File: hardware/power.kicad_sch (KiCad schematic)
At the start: 61 parts, among them IC1 LMR38020FDDAR, Q1 LMR51635XDDCR, Q2 LMR51635XDDCR, U3 LM1117-3.3

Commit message: Table updated- fuses and conns still not added
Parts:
- C10, C11, C13, C14, C15, C26, C30, C31: Mouser Price/Stock (none) -> https://www.mouser.pl/ProductDetail/KEMET/C0603C104J5RACTM?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
- C12, C19, C24, C25, C32, C33: Mouser Price/Stock (none) -> https://www.mouser.pl/ProductDetail/Murata-Electronics/GRM3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
- C16, C17, C27, C28, C29, C5: Mouser Price/Stock (none) -> https://www.mouser.pl/ProductDetail/TAIYO-YUDEN/MMJCG168CB7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
- C20, C22: footprint Capacitor_SMD:CP_Elec_4x5.8 -> SamacSys_Parts:CAPPM7343X310N; Mouser Price/Stock https://www.mouser.pl/ProductDetail/Samsung-Electro-Mechani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 -> https://www.mouser.pl/ProductDetail/TDK/C2012X5R1V226M125AC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
- C21, C23, C9: Mouser Price/Stock (none) -> https://www.mouser.pl/ProductDetail/Murata-Electronics/GRM1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
- D2: Mouser Price/Stock (none) -> https://www.mouser.pl/ProductDetail/Diotec-Semiconductor/SK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
- D3, D4: Mouser Price/Stock (none) -> https://www.we-online.com/components/products/datasheet/150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
- L1: Mouser Price/Stock (none) -> https://www.mouser.pl/ProductDetail/Bourns/SRU1028A-150Y?qs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
- L2, L3: Mouser Price/Stock (none) -> https://www.mouser.pl/ProductDetail/Bourns/SRR1206-120ML?qs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
- Q1, Q2: Mouser Price/Stock (none) -> https://www.mouser.pl/ProductDetail/Texas-Instruments/LMR51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
- R10: Mouser Price/Stock (none) -> https://www.mouser.pl/ProductDetail/Vishay-Dale/CRCW060310K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
- R11, R13: Mouser Price/Stock (none) -> https://www.mouser.pl/ProductDetail/YAGEO/AC0603DRE0713K7L?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
- R12, R5: Mouser Price/Stock (none) -> https://www.mouser.pl/ProductDetail/KOA-Speer/RK73B1JTTD104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
- R14, R8: Mouser Price/Stock (none) -> https://www.mouser.pl/ProductDetail/Vishay-Dale/CRCW06031K0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
- R7: Mouser Price/Stock (none) -> https://www.mouser.pl/ProductDetail/Vishay-Beyschlag/MCT060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
- R9: Mouser Price/Stock (none) -> https://www.mouser.pl/ProductDetail/Panasonic/ERJ-S03F4022V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
- U3: Mouser Price/Stock (none) -> https://www.mouser.pl/ProductDetail/Texas-Instruments/LM111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

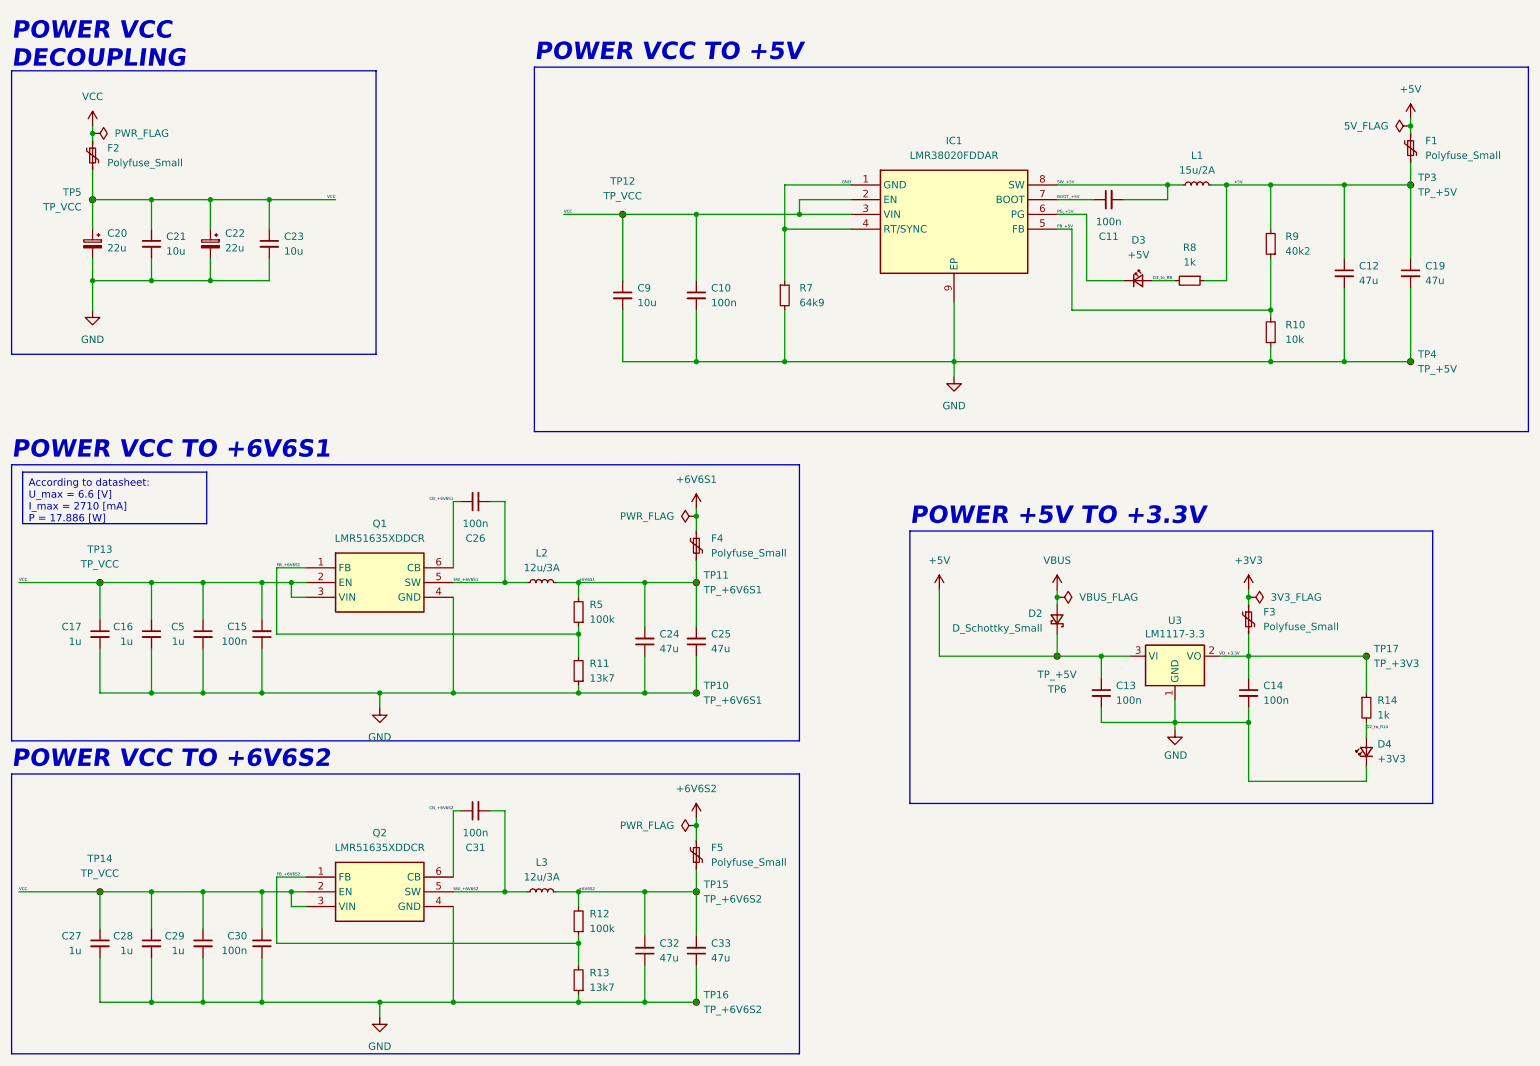
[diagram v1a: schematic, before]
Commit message: All footprints added
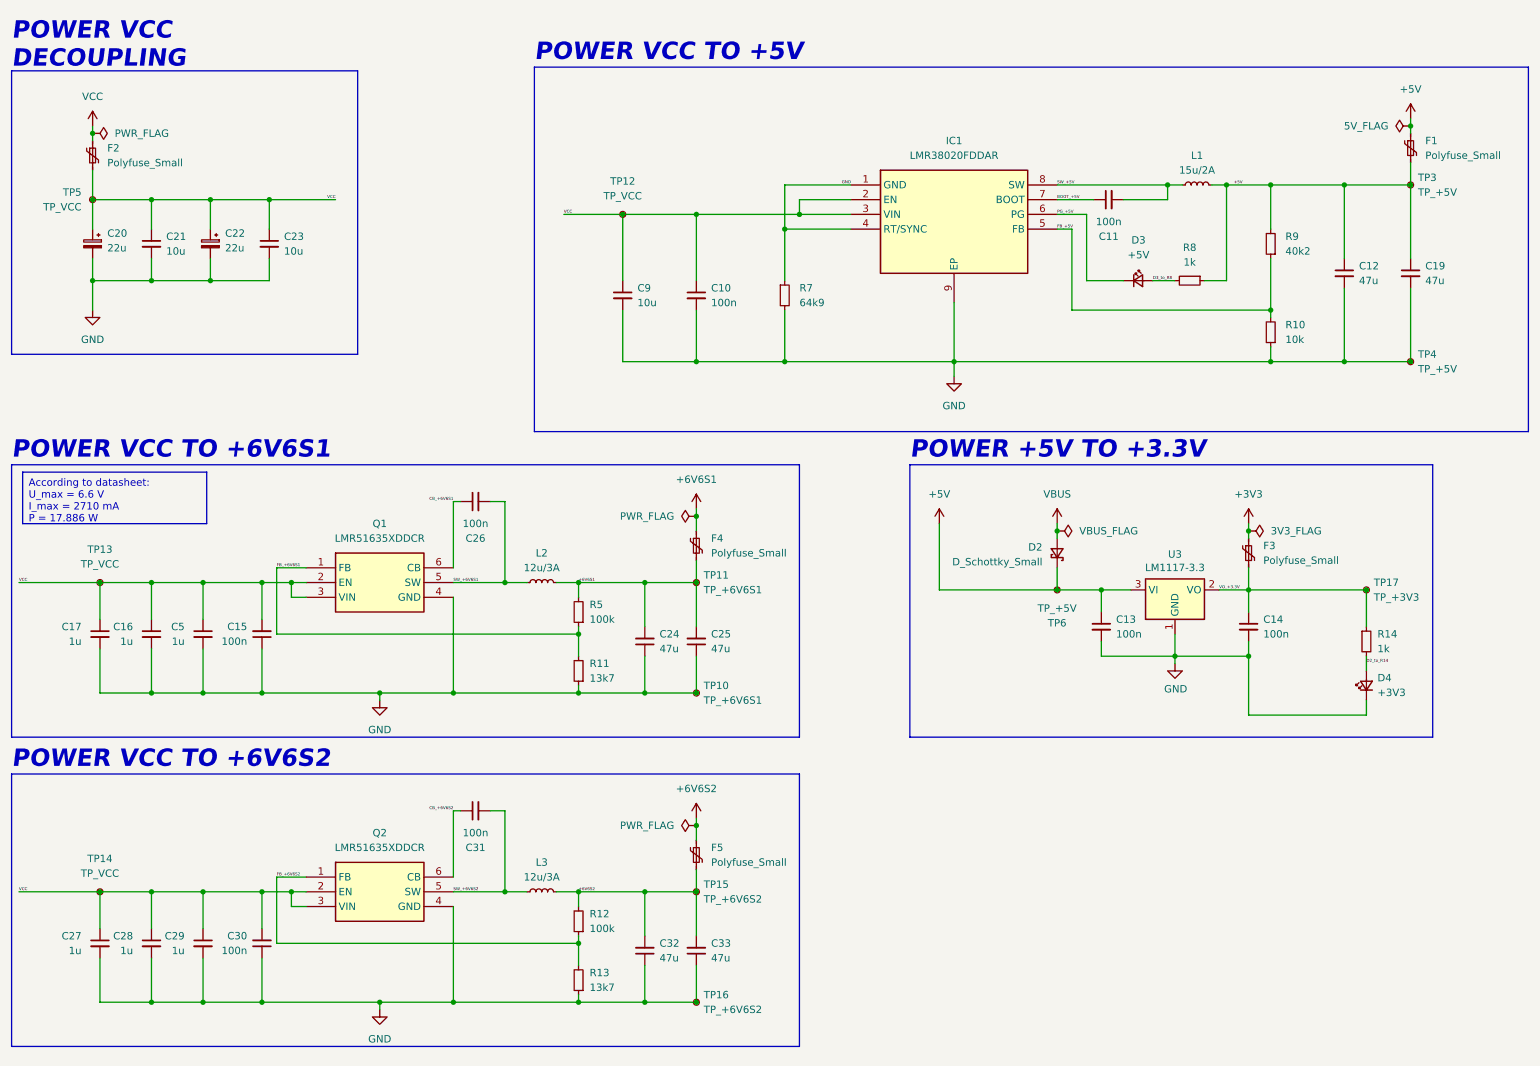
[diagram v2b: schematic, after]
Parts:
- F1, F3: footprint Fuse:Fuse_1206_3216Metric -> SamacSys_Parts:MINIASMDC260F162; Mouser Price/Stock (none) -> https://www.mouser.pl/ProductDetail/Littelfuse/MINIASMDC260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
- F2: footprint Fuse:Fuse_1206_3216Metric -> Fuse:Fuse_1206_3216Metric_Pad1.42x1.75mm_HandSolder; Mouser Price/Stock (none) -> https://www.mouser.pl/ProductDetail/Bourns/SF-1206HH800R-2?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
- F4, F5: footprint Fuse:Fuse_1206_3216Metric -> Fuse:Fuse_1206_3216Metric_Pad1.42x1.75mm_HandSolder; Mouser Price/Stock (none) -> https://www.mouser.pl/ProductDetail/Littelfuse/1206L150THWR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
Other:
- moved on the sheet: C13, C14, D2, D4, F3, R14, TP17, TP6, U3

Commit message: pcb scheme update - general/basic aligment
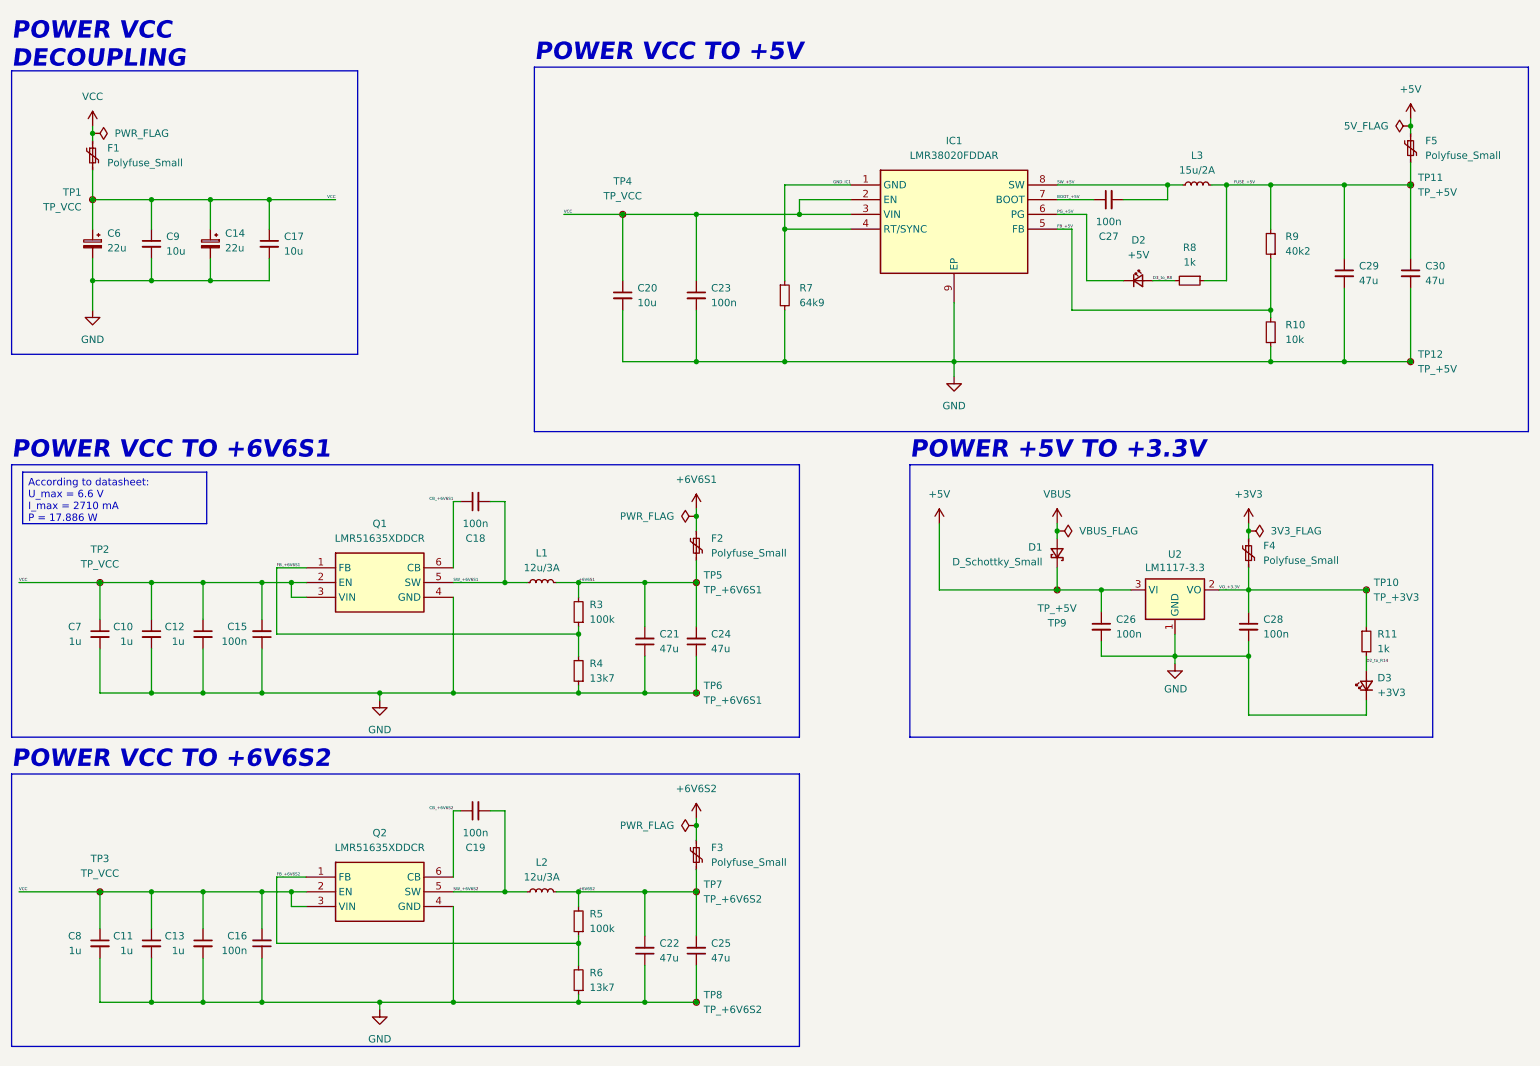
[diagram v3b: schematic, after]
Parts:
- F2: renamed from F4; footprint Fuse:Fuse_1206_3216Metric_Pad1.42x1.75mm_HandSolder -> Fuse:Fuse_0805_2012Metric_Pad1.15x1.40mm_HandSolder; Mouser Price/Stock https://www.mouser.pl/ProductDetail/Littelfuse/1206L150THWR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 -> https://www.mouser.pl/ProductDetail/Eaton-Electronics/PTSLR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
- F3: renamed from F5; footprint Fuse:Fuse_1206_3216Metric_Pad1.42x1.75mm_HandSolder -> Fuse:Fuse_0805_2012Metric_Pad1.15x1.40mm_HandSolder; Mouser Price/Stock https://www.mouser.pl/ProductDetail/Littelfuse/1206L150THWR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 -> https://www.mouser.pl/ProductDetail/Eaton-Electronics/PTSLR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
- L1: renamed from L2; footprint SamacSys_Parts:SRR1206120ML -> SamacSys_Parts:VLS6045; Mouser Price/Stock https://www.mouser.pl/ProductDetail/Bourns/SRR1206-120ML?qs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 -> https://www.mouser.pl/ProductDetail/TDK/VLS6045EX-150M?qs=o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
- L2: renamed from L3; footprint SamacSys_Parts:SRR1206120ML -> SamacSys_Parts:VLS6045; Mouser Price/Stock https://www.mouser.pl/ProductDetail/Bourns/SRR1206-120ML?qs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 -> https://www.mouser.pl/ProductDetail/TDK/VLS6045EX-150M?qs=o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
- L3: renamed from L1; footprint Inductor_SMD:L_Bourns-SRU1028_10.0x10.0mm -> SamacSys_Parts:VLS6045; Mouser Price/Stock https://www.mouser.pl/ProductDetail/Bourns/SRU1028A-150Y?qs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 -> https://www.mouser.pl/ProductDetail/TDK/VLS6045EX-150M?qs=o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
- renumbered C16 to C10, C28 to C11, C5 to C12, C29 to C13, C22 to C14, C30 to C16, C23 to C17, C26 to C18, C31 to C19, C9 to C20, C24 to C21, C32 to C22, C10 to C23, C25 to C24, C33 to C25, C13 to C26, C11 to C27, C14 to C28, C12 to C29, C19 to C30, C20 to C6, C17 to C7, C27 to C8, C21 to C9, D2 to D1, D3 to D2, D4 to D3, F2 to F1, F3 to F4, F1 to F5, R14 to R11, R5 to R3, R11 to R4, R12 to R5, R13 to R6, TP5 to TP1, TP17 to TP10, TP3 to TP11, TP4 to TP12, TP13 to TP2, TP14 to TP3, TP12 to TP4, TP11 to TP5, TP10 to TP6, TP15 to TP7, TP16 to TP8, TP6 to TP9, U3 to U2
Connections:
- net +5V: no longer C29.1, C30.1, F5.2, L3.2, R8.1, R9.2, TP11.1
- net GND: no longer IC1.1 (GND), IC1.4 (RT/SYNC), R7.1
- new net FUSE_+5V: C29.1, C30.1, F5.2, L3.2, R8.1, R9.2, TP11.1
- new net GND_IC1: IC1.1 (GND), IC1.4 (RT/SYNC), R7.1

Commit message: Items assebled
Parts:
- TP9: value TP_+5V -> T_+5V
- renumbered TP1 to T1, TP10 to T10, TP11 to T11, TP12 to T12, TP2 to T2, TP3 to T3, TP4 to T4, TP5 to T5, TP6 to T6, TP7 to T7, TP8 to T8
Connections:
- net +6V6S1: no longer C21.2, C24.2, F2.2, L1.2, R3.2, T5.1
- net +6V6S2: no longer C22.2, C25.2, F3.2, L2.2, R5.2, T7.1
- net VCC: no longer C14.1, C17.1, C6.1, C9.1, F1.2, T1.1
- new net +6V6S1_OUT: C21.2, C24.2, F2.2, L1.2, R3.2, T5.1
- new net +6V6S2_OUT: C22.2, C25.2, F3.2, L2.2, R5.2, T7.1
- new net VCC_IN: C14.1, C17.1, C6.1, C9.1, F1.2, T1.1
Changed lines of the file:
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@@
 		)
 	)
-	(label "VCC"
+	(label "VCC_IN"
 		(at 72.39 48.26 180)
 		(effects
@@
 		)
 	)
-	(label "+6V6S2"
+	(label "+6V6S2_OUT"
 		(at 114.3 167.64 0)
 		(effects
@@
 		)
 	)
-	(label "+6V6S1"
+	(label "+6V6S1_OUT"
 		(at 114.3 114.3 0)
 		(effects
@@
 			)
 		)
-		(property "Value" "TP_+5V"
+		(property "Value" "T_+5V"
 			(at 196.85 118.745 90)
 			(effects
@@
 		(dnp no)
 		(fields_autoplaced yes)
-		(property "Reference" "TP10"
+		(property "Reference" "T10"
 			(at 251.46 114.2999 0)
 			(effects
@@
 			(project "drs"
 				(path "/b652b05a-4e3d-4ad1-b032-18886abe7d45/29f85ecd-7b45-4817-8022-029f79a199a0"
-					(reference "TP10")
+					(reference "T10")
 					(unit 1)
 				)
@@
 		(on_board yes)
 		(dnp no)
-		(property "Reference" "TP1"
+		(property "Reference" "T1"
 			(at 28.575 46.9899 0)
 			(effects
@@
 			(project "drs"
 				(path "/b652b05a-4e3d-4ad1-b032-18886abe7d45/29f85ecd-7b45-4817-8022-029f79a199a0"
-					(reference "TP1")
+					(reference "T1")
 					(unit 1)
 				)
@@
 		(dnp no)
 		(fields_autoplaced yes)
-		(property "Reference" "TP8"
+		(property "Reference" "T8"
 			(at 135.89 185.4199 0)
 			(effects
@@
 			(project "drs"
 				(path "/b652b05a-4e3d-4ad1-b032-18886abe7d45/29f85ecd-7b45-4817-8022-029f79a199a0"
-					(reference "TP8")
+					(reference "T8")
 					(unit 1)
 				)
@@
 		(dnp no)
 		(fields_autoplaced yes)
-		(property "Reference" "TP12"
+		(property "Reference" "T12"
 			(at 259.08 74.9299 0)
 			(effects
@@
 			(project "drs"
 				(path "/b652b05a-4e3d-4ad1-b032-18886abe7d45/29f85ecd-7b45-4817-8022-029f79a199a0"
-					(reference "TP12")
+					(reference "T12")
 					(unit 1)
 				)
@@
 		(dnp no)
 		(fields_autoplaced yes)
-		(property "Reference" "TP3"
-			(at 31.75 161.925 90)
+		(property "Reference" "T3"
+			(at 31.75 162.56 90)
 			(effects
 				(font
@@
 		)
 		(property "Value" "TP_VCC"
-			(at 31.75 164.465 90)
+			(at 31.75 165.1 90)
 			(effects
 				(font
@@
 			(project "drs"
 				(path "/b652b05a-4e3d-4ad1-b032-18886abe7d45/29f85ecd-7b45-4817-8022-029f79a199a0"
-					(reference "TP3")
+					(reference "T3")
 					(unit 1)
 				)
@@
 		(dnp no)
 		(fields_autoplaced yes)
-		(property "Reference" "TP4"
-			(at 121.92 45.085 90)
+		(property "Reference" "T4"
+			(at 121.92 45.72 90)
 			(effects
 				(font
@@
 		)
 		(property "Value" "TP_VCC"
-			(at 121.92 47.625 90)
+			(at 121.92 48.26 90)
 			(effects
 				(font
@@
 			(project "drs"
 				(path "/b652b05a-4e3d-4ad1-b032-18886abe7d45/29f85ecd-7b45-4817-8022-029f79a199a0"
-					(reference "TP4")
+					(reference "T4")
 					(unit 1)
 				)
@@
 		(dnp no)
 		(fields_autoplaced yes)
-		(property "Reference" "TP7"
+		(property "Reference" "T7"
 			(at 135.89 166.3699 0)
 			(effects
@@
 			(project "drs"
 				(path "/b652b05a-4e3d-4ad1-b032-18886abe7d45/29f85ecd-7b45-4817-8022-029f79a199a0"
-					(reference "TP7")
+					(reference "T7")
 					(unit 1)
 				)
@@
 		(dnp no)
 		(fields_autoplaced yes)
-		(property "Reference" "TP6"
+		(property "Reference" "T6"
 			(at 135.89 132.0799 0)
 			(effects
@@
 			(project "drs"
 				(path "/b652b05a-4e3d-4ad1-b032-18886abe7d45/29f85ecd-7b45-4817-8022-029f79a199a0"
-					(reference "TP6")
+					(reference "T6")
 					(unit 1)
 				)
@@
 		(dnp no)
 		(fields_autoplaced yes)
-		(property "Reference" "TP2"
-			(at 31.75 108.585 90)
+		(property "Reference" "T2"
+			(at 31.75 109.22 90)
 			(effects
 				(font
@@
 		)
 		(property "Value" "TP_VCC"
-			(at 31.75 111.125 90)
+			(at 31.75 111.76 90)
 			(effects
 				(font
@@
 			(project "drs"
 				(path "/b652b05a-4e3d-4ad1-b032-18886abe7d45/29f85ecd-7b45-4817-8022-029f79a199a0"
-					(reference "TP2")
+					(reference "T2")
 					(unit 1)
 				)
@@
 		(dnp no)
 		(fields_autoplaced yes)
-		(property "Reference" "TP11"
+		(property "Reference" "T11"
 			(at 259.08 44.4499 0)
 			(effects
@@
 			(project "drs"
 				(path "/b652b05a-4e3d-4ad1-b032-18886abe7d45/29f85ecd-7b45-4817-8022-029f79a199a0"
-					(reference "TP11")
+					(reference "T11")
 					(unit 1)
 				)
@@
 		(dnp no)
 		(fields_autoplaced yes)
-		(property "Reference" "TP5"
+		(property "Reference" "T5"
 			(at 135.89 113.0299 0)
 			(effects
@@
 			(project "drs"
 				(path "/b652b05a-4e3d-4ad1-b032-18886abe7d45/29f85ecd-7b45-4817-8022-029f79a199a0"
-					(reference "TP5")
+					(reference "T5")
 					(unit 1)
 				)
